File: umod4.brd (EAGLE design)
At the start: 104.9 x 71.1 mm, 89 parts, among them IC3 27C256-FEED-THRU, J1 DMSAT-SF-PEJ, J2 10118194-0001LF, J4 CORTEX_DEBUG-PTH, J5 C160394/JST BM08B-SRSS, M1 RPi Pico W, M2 Generic single-sided NEO-8, Q1 C10487/SI2301CDS, Q2 C2150/SS8050, U1 C113281/74LVC541, U2 C6091/74LVC4245, U3 C113281/74LVC541, U4 C2040/RP2040, U5 C97521/W25Q128JVSIQ, U6 C10428/74LVC2G04, U7 C10428/74LVC2G04, U8 WS2812C-2020, U9 TPS560430X, Y1 C9002/12MHz

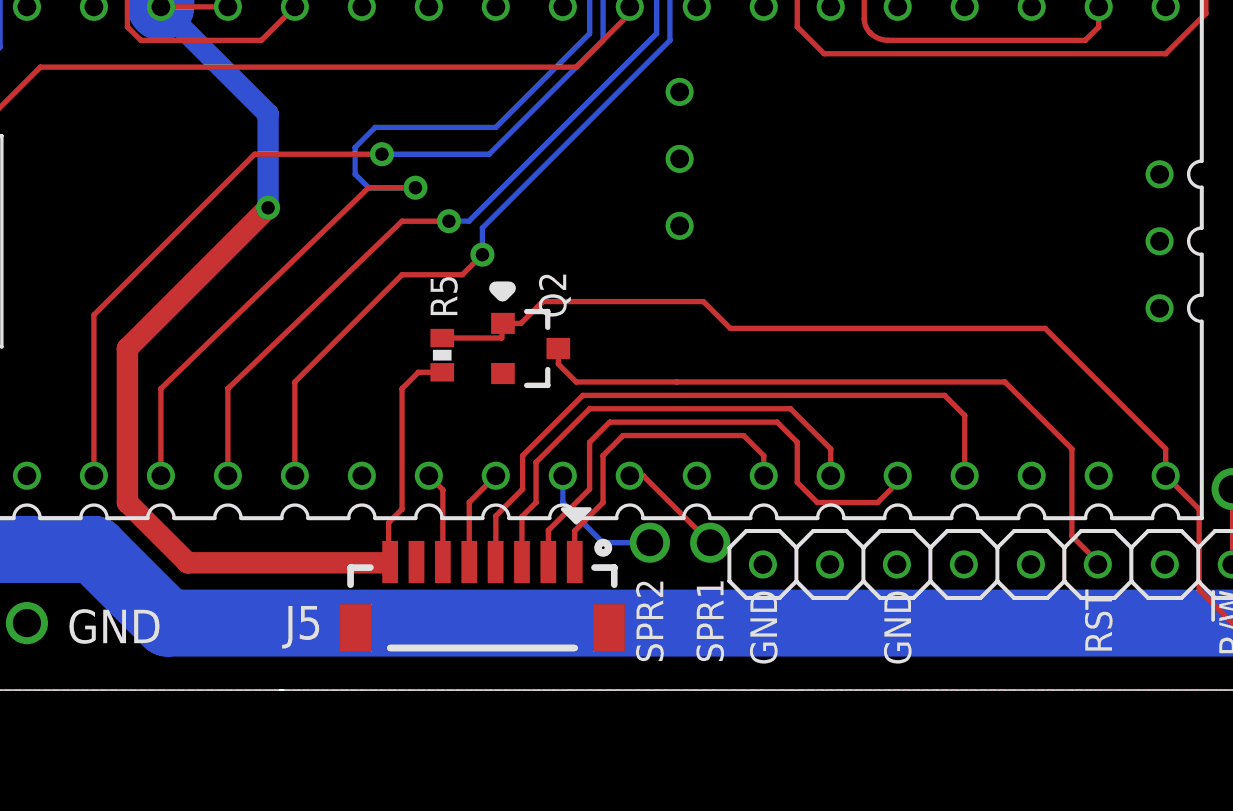
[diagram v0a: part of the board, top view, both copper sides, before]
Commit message: Flipped J5 for easier hand soldering
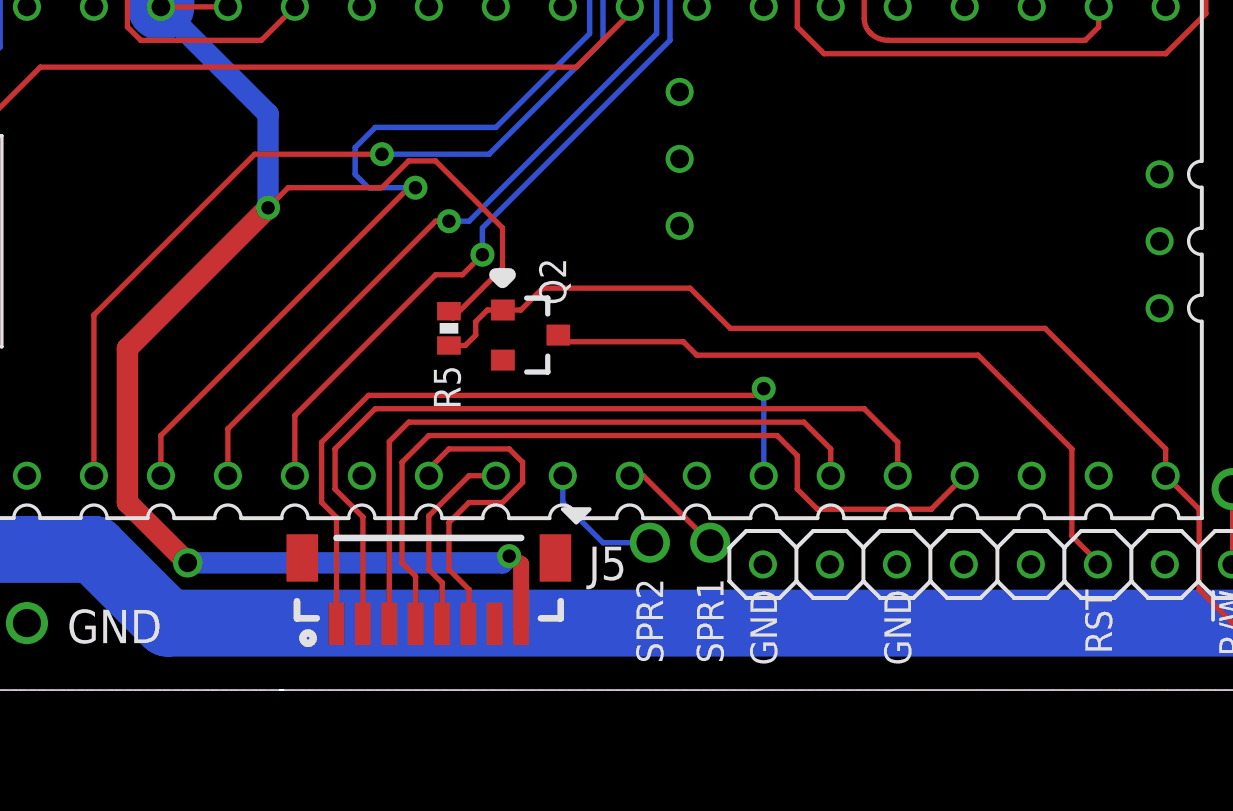
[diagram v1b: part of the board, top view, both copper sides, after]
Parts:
- moved J5 2.05 mm to (33.5, 3.81), turned to 0 degrees
- moved R5 1.05 mm to (34.3, 13.7), turned to 90 degrees
- moved Q2 0.51 mm to (37.3, 13.5)
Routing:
- net SPI1_SCK: track 12.0 -> 28.0 mm, vias 0 -> 1
- net +3V3: track 338.0 -> 352.0 mm, vias 11 -> 13
- net SPI1_MISO: track 19.9 -> 30.8 mm
- net LCD_BKLT: track 3.49 -> 12.7 mm
- net SPI1_MOSI: track 17.7 -> 25.4 mm
- net SPI1_CS: track 24.8 -> 30.5 mm
- net LCD_DC: track 3.69 -> 7.48 mm
- net RP_SWD: track 133.9 -> 132.9 mm
- net PICOW_U1_TX: track 109.0 -> 108.2 mm
- net PICOW_U1_RX: track 108.7 -> 108.0 mm

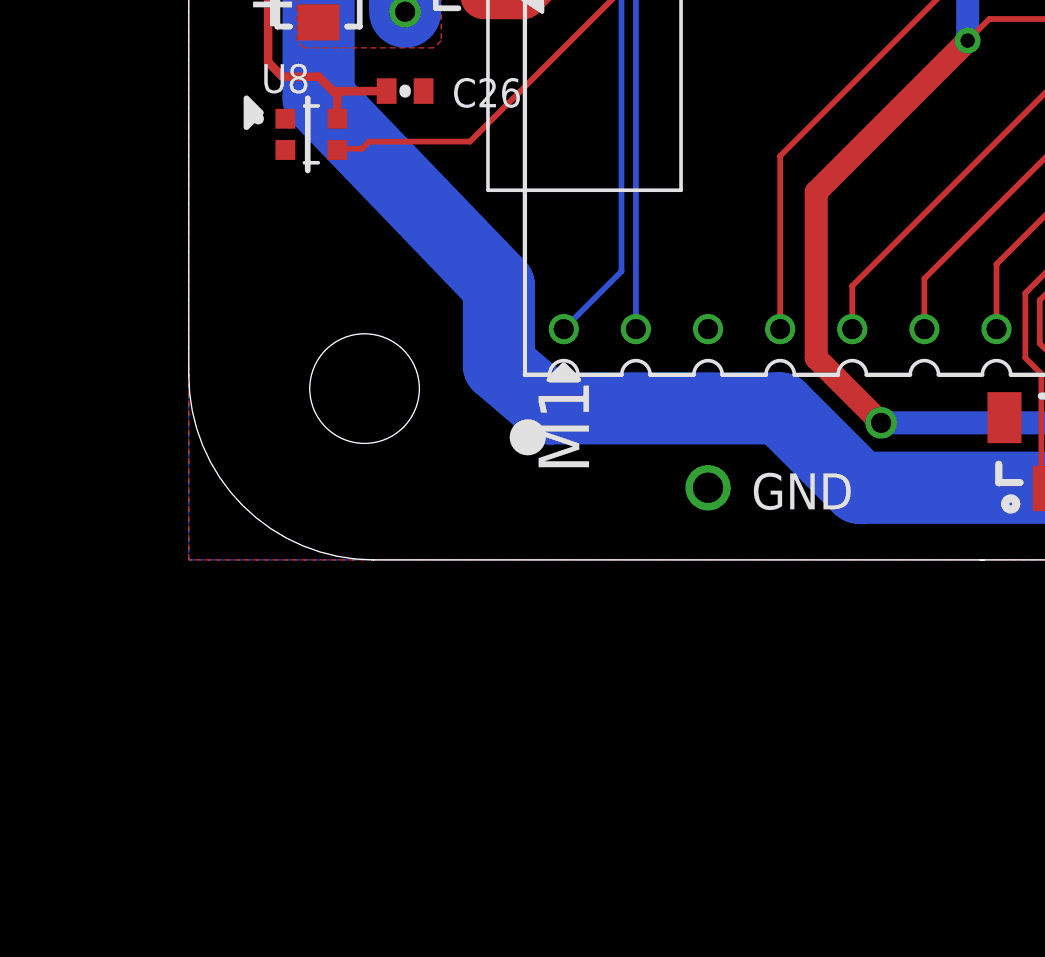
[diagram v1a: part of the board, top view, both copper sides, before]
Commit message: Updated all LSCS part attributes
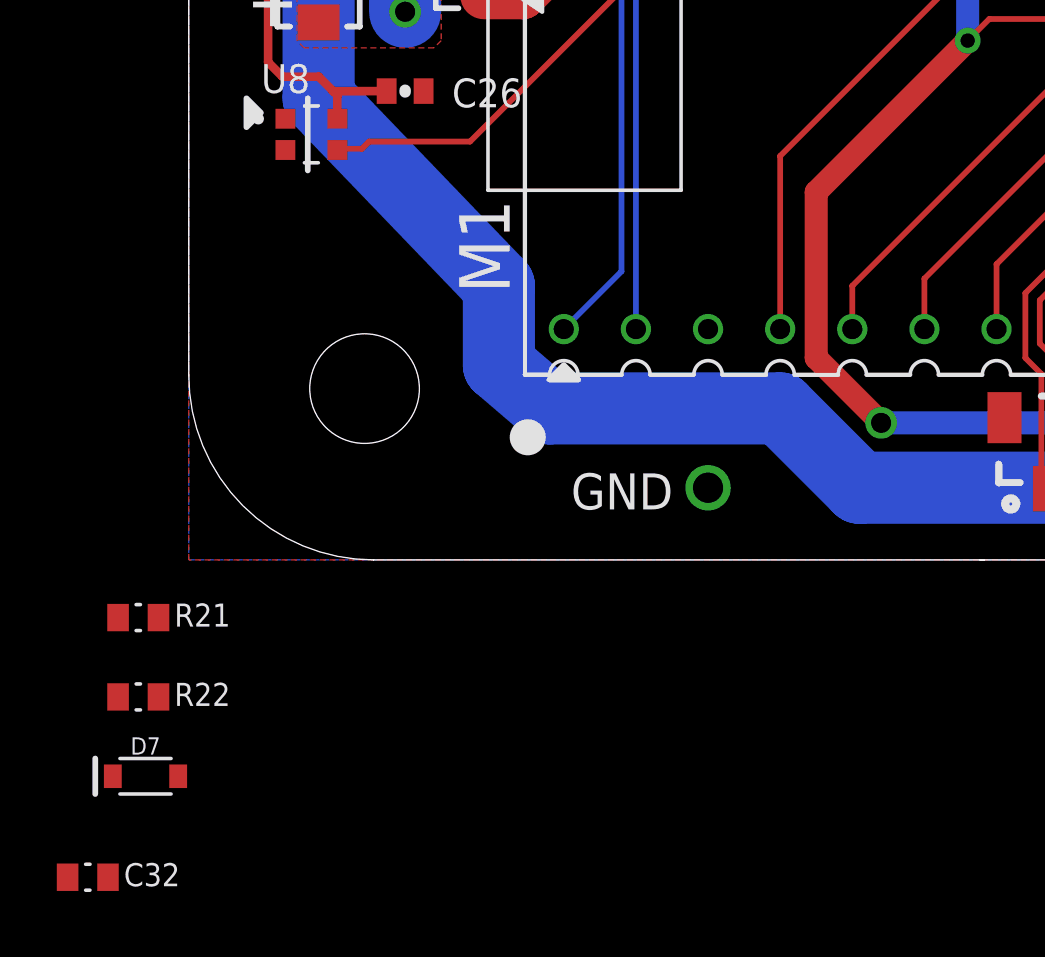
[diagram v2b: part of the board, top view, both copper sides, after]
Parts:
- added C32: 1nF/25V, robins-v7:SMD-0603
- added D7: 1N5819WS, SparkFun-DiscreteSemi:SOD-323
- added R21: 20K, robins-v7:SMD-0603
- added R22: 5K1, robins-v7:SMD-0603
- C1, C10, C11, C12, C14, C15, C16, C19, C23, C24, C25, C26, C3, C5, C6, C7, C8, C9: value C1525/100n/10V/X7R -> 100n/10V/X7R
- C17, C18: value C1562/33p/6.3V/COG -> 33p/6.3V/COG
- C2, C4: value C52923/1u/25V/X5R -> 1u/25V/X5R
- C20, C21, C22: value C12530/2u2/6.3V/X5R -> 2u2/6.3V/X5R
- C27: value C368809/4u7/10V/X5R -> 4u7/10V/X5R
- D2: value C72043/Green -> Green
- D3, D4: value 1A/23V/620mV -> 1N5819WS
- J5: value C160394/JST BM08B-SRSS -> JST BM08B-SRSS
- Q2: value C2150/SS8050 -> SS8050
- R1, R12, R14, R15, R16, R3, R5, R6, R8: value C25744/10K -> 10K
- R10, R11, R18: value C25100/27R -> 27R
- R13, R4: value C11702/1K -> 1K
- R2: value C25905/5K1 -> 5K1
- R7: value C25117/470R -> 470R
- U1, U3: value C113281/74LVC541 -> 74LVC541
- U2: value C6091/74LVC4245 -> 74LVC4245
- U4: value C2040/RP2040 -> RP2040
- U5: value C97521/W25Q128JVSIQ -> W25Q128JVSIQ
- U6, U7: value C10428/74LVC2G04 -> 74LVC2G04
- U9: value TPS560430X -> LGS5148
- Y1: value C9002/12MHz -> 12MHz
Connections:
- new net VIN_MEAS: C32.P$1, D7.A, R21.P$1, R22.P$2
- net +3V3: now also D7.C
- net GND: now also C32.P$2, R22.P$1
- net VIN: now also R21.P$2

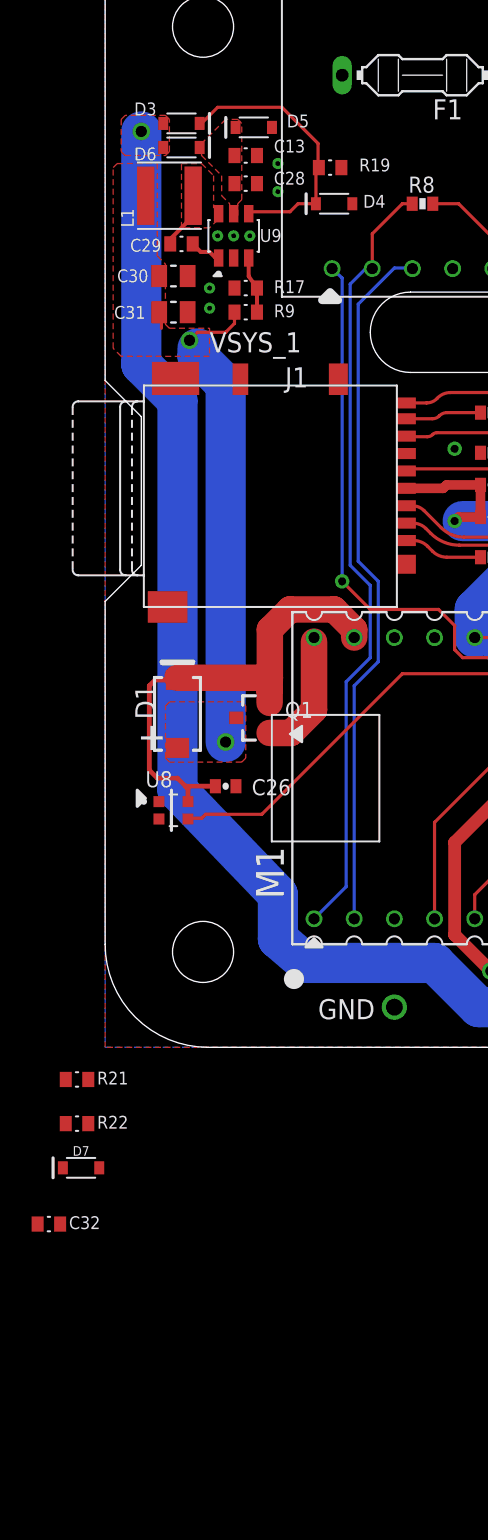
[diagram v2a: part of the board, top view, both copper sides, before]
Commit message: More updates to add LCSC part numbers
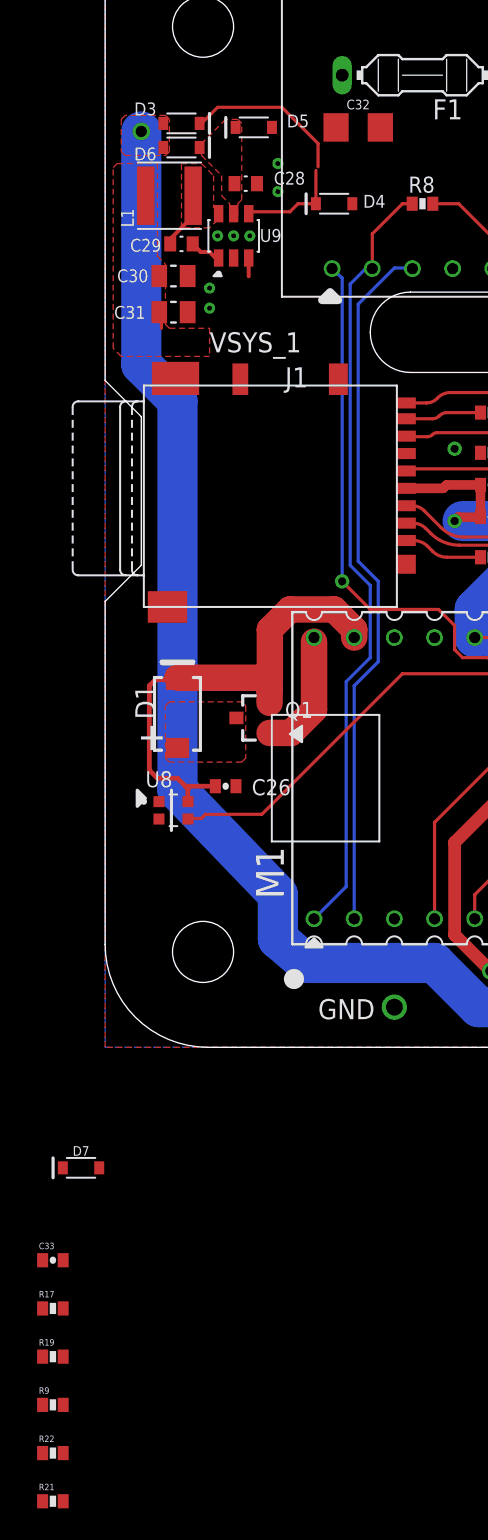
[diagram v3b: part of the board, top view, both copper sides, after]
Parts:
- removed C13: 4.7uF/25V, robins-v7:SMD-0603
- added C33: 100n/16V/X7R, SparkFun-03-01-2010:0402-CAP
- C1, C10, C11, C12, C14, C15, C16, C19, C23, C24, C25, C26, C3, C5, C6, C7, C8, C9: value 100n/10V/X7R -> 100n/16V/X7R
- C28, C29: value 0.1uF/25V -> 100n/50V/X7R
- C32: value 1nF/25V -> 4u7/50V/X7R; device robins-v7:SMD-0603 -> SparkFun-Capacitors:1206
- R17: value 22K -> 10K; device robins-v7:SMD-0603 -> SparkFun-03-01-2010:0402-RES
- R19, R21, R22: device robins-v7:SMD-0603 -> SparkFun-03-01-2010:0402-RES
- R9: value 51K -> 56K; device robins-v7:SMD-0603 -> SparkFun-03-01-2010:0402-RES
- moved R19 77.2 mm to (-3.30, -19.6), turned to 0 degrees
- moved C32 72.0 mm to (16.0, 58.2)
- moved R9 70.2 mm to (-3.30, -22.6), turned to 0 degrees
- moved R17 65.7 mm to (-3.30, -16.5)
- moved R21 26.7 mm to (-3.30, -28.7)
- moved R22 20.9 mm to (-3.30, -25.7)
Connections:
- net GND: now also C32.2, C33.2; no longer C13.P$2, C32.P$2, R17.P$1, R19.P$1, R22.P$1
- net N$16: no longer R17.P$2, R9.P$1
- net N$23: no longer R19.P$2
- net VIN: now also C32.1, R21.1; no longer C13.P$1, R21.P$2
- net VIN_MEAS: now also C33.1, R21.2; no longer C32.P$1, R21.P$1, R22.P$2
- net VSYS_1: no longer R9.P$2
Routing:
- net VSYS_1: track 31.4 -> 1.07 mm, vias 2 -> 0
- net N$16: track 3.59 -> 1.16 mm

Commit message: Before renumbering components
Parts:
- added C13: 100n/16V/X7R, SparkFun-03-01-2010:0402-CAP
- C30, C31: value 10uF/10V -> 10uF/25V/X5R
- D1: value C22452/SS54 -> 1N5819WS; device SparkFun-DiscreteSemi:SMA-DIODE -> SparkFun-DiscreteSemi:SOD-323
- D5, D6: value 1A/23V/620mV -> 1N5819WS
- moved R21 88.9 mm to (15.5, 58.2)
- moved R17 71.6 mm to (15.5, 52.6)
- moved R22 69.9 mm to (37.3, 31.2), turned to 90 degrees
- moved R9 69.6 mm to (8.38, 46.0)
- moved R19 68.1 mm to (8.38, 47.5), turned to 180 degrees
- moved C33 59.1 mm to (35.3, 31.2), turned to 90 degrees
- moved D7 50.0 mm to (30.5, 30.7)
- moved R5 11.6 mm to (40.4, 3.81), turned to 270 degrees
- moved D3 11.4 mm to (16.0, 56.1), turned to 0 degrees
- moved Q2 11.1 mm to (43.2, 4.06), turned to 180 degrees
- moved JP2 9.52 mm to (36.3, 38.9), turned to 270 degrees
- moved C32 5.73 mm to (10.4, 56.9)
- moved D5 4.77 mm to (13.7, 60.2)
- moved R8 3.89 mm to (23.9, 52.6)
- moved C26 3.05 mm to (4.57, 16.5), turned to 180 degrees
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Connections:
- removed net N$23: D3.C, D4.C, U9.4
- removed net SPARE1: M1.12
- removed net SPARE2: M1.11
- removed net SPARE3: M1.27
- new net EN: D3.C, D4.C, R17.1, U9.4
- net +3V3: now also C13.1
- net EP_RUN: now also M1.27; no longer M1.32
- net GND: now also C13.2, R17.2, R19.2, R22.2
- net GPS_PPS: now also M1.12; no longer M1.34
- net KEEP_ALIVE: now also M1.11
- net N$16: now also R19.1, R9.2
- net SPARE0: now also M1.34; no longer M1.31
- net VIN_MEAS: now also M1.32, R22.1
- net VSYS_1: now also R9.1
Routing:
- net KEEP_ALIVE: track 0.00 -> 80.0 mm, vias 0 -> 1
- net VIN_MEAS: track 0.00 -> 59.4 mm, vias 0 -> 2
- net GPS_PPS: track 36.9 -> 70.3 mm, vias 1 -> 2
- net VSYS_1: track 1.07 -> 29.7 mm, vias 0 -> 2
- net +5_ECU: track 169.6 -> 189.1 mm
- net +12_US: track 0.00 -> 18.3 mm
- net N$23: track 17.1 -> 0.00 mm
- net EP_RUN: track 113.9 -> 97.9 mm
- net +3V3: track 352.0 -> 337.9 mm, vias 13 -> 11
- net !RESET!_5V: track 26.1 -> 16.5 mm
- net EN: track 0.00 -> 9.38 mm
- net PICOW_U1_TX: track 108.2 -> 115.8 mm
- net !RESET!_HC11_OUT: track 131.1 -> 123.6 mm
- net PICOW_U1_RX: track 108.0 -> 115.4 mm
- net SPARE2: track 4.95 -> 0.00 mm, vias 1 -> 0
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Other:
- outline, holes or cut-outs redrawn
- board text removed: "SPR1"
- board text removed: "SPR2"

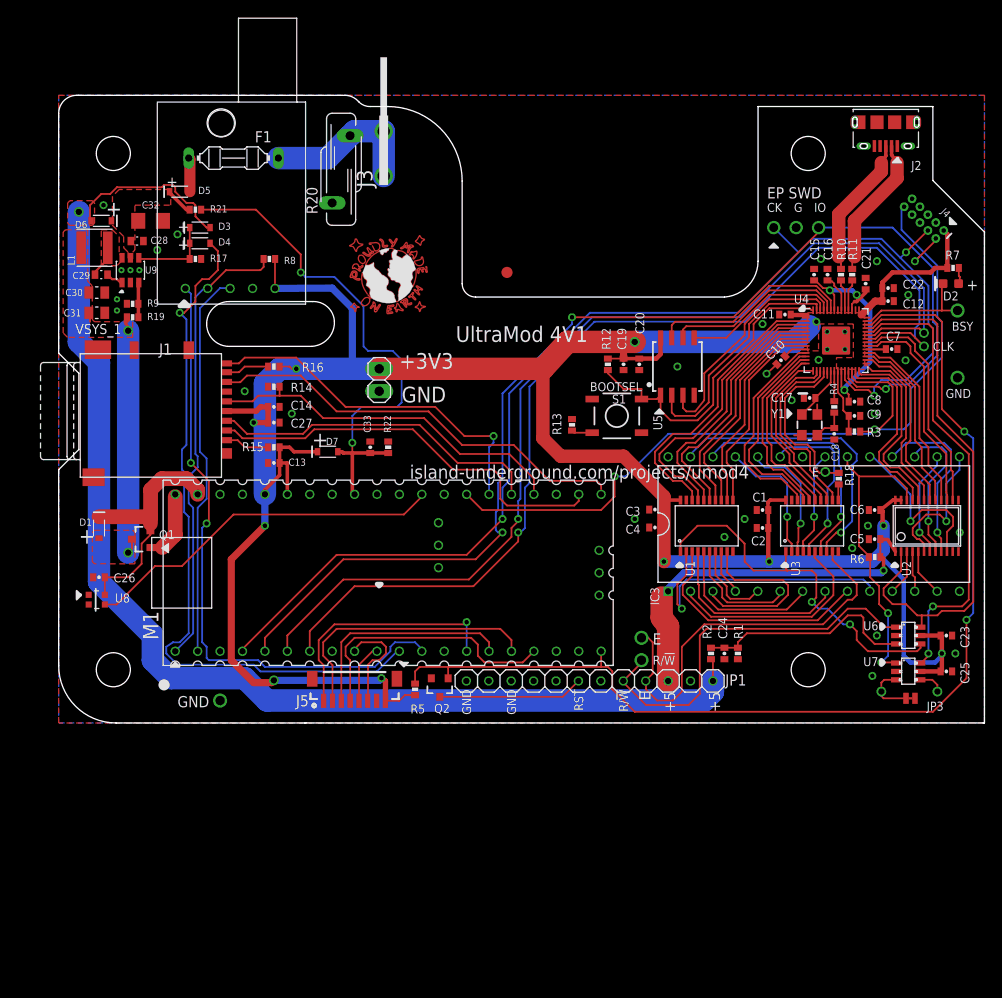
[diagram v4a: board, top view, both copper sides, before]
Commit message: PCB Updates as per ChangeList.md
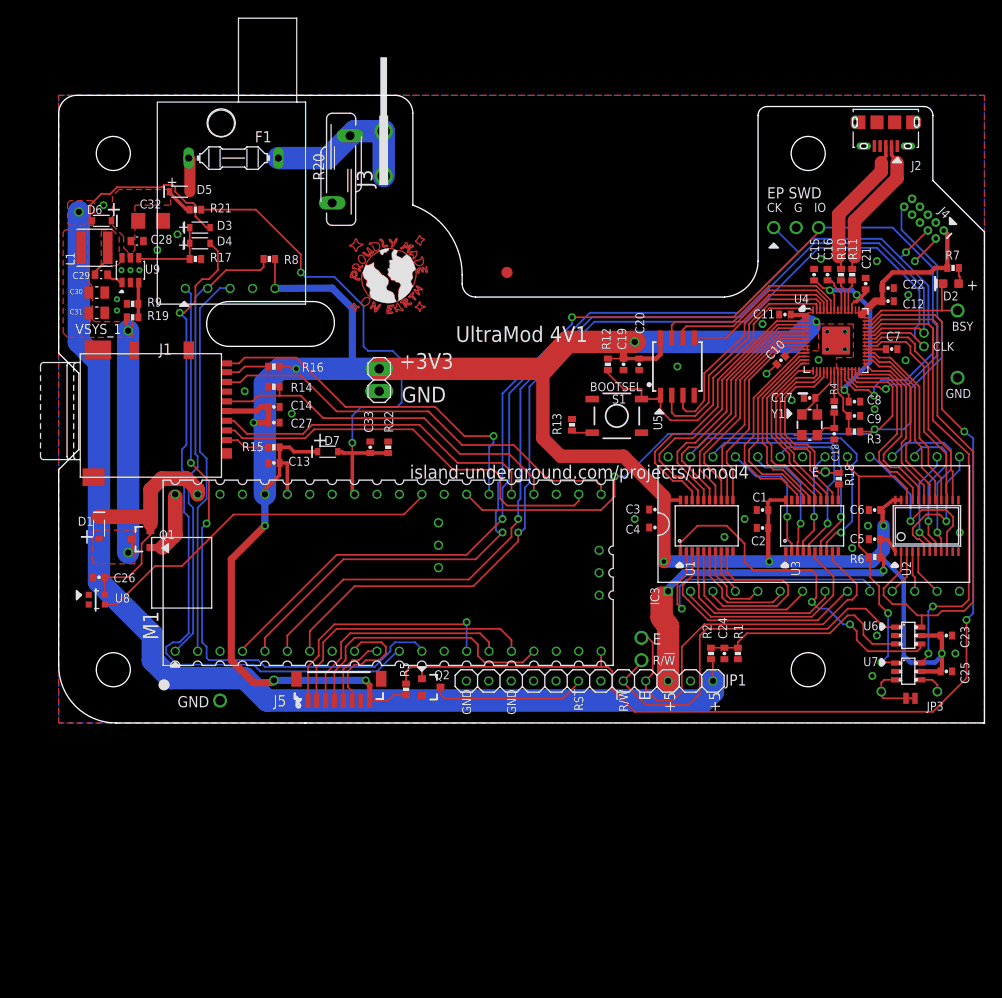
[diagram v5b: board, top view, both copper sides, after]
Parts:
- moved J5 1.78 mm to (31.8, 3.81)
- moved R5 1.02 mm to (39.4, 3.81)
- moved Q2 1.02 mm to (42.2, 4.06), turned to 270 degrees
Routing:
- net LCD_BKLT: track 11.8 -> 13.8 mm
- net LCD_DC: track 6.76 -> 8.24 mm
- net +3V3: track 337.9 -> 336.5 mm
- net !RESET!_5V: track 16.5 -> 17.6 mm
- net !RESET!_HC11_OUT: track 123.6 -> 124.7 mm
- net SPI1_MOSI: track 25.2 -> 26.0 mm
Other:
- outline, holes or cut-outs redrawn
